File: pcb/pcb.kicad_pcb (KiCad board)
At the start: 2 copper layers, 55 x 70 mm, 61 parts, among them J1 SW, J2 HEATER, J3 FAN, J4 BME280, J5 DISPLAY, J6 NTC, J7 POWER, Q1 IRFR9024NTRPBF, Q2 2n3904S-RTK/PS_C18536, Q3 2n3904S-RTK/PS_C18536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

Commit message: Work with schematics and pcb. update *.ioc files at project.
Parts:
- removed C13: 100uf, Capacitor_THT:CP_Radial_D8.0mm_P5.00mm
- added H1: MountingHole, MountingHole:MountingHole_3.2mm_M3_DIN965_Pad, F.Cu at (94.2, 54.0)
- added H2: MountingHole, MountingHole:MountingHole_3.2mm_M3_DIN965_Pad, F.Cu at (62.0, 53.8)
- added H3: MountingHole, MountingHole:MountingHole_3.2mm_M3_DIN965_Pad, F.Cu at (95.1, 126.2)
- added H4: MountingHole, MountingHole:MountingHole_3.2mm_M3_DIN965_Pad, F.Cu at (61.6, 126.2)
- C10, C11, C12, C15, C16, C17, C6, C7, C9, R17, R18, R19, R4, U1, Y1: moved to B.Cu
- Q4, R16, R20, R6, R7: moved to F.Cu
- moved J4 49.7 mm to (60.5, 99.0)
- moved J6 44.9 mm to (95.1, 99.2), turned to 90 degrees
- moved R15 32.9 mm to (69.1, 98.7), turned to -90 degrees
- moved R6 29.5 mm to (72.7, 79.9), turned to 180 degrees
- moved R16 28.5 mm to (84.8, 104.0), turned to 180 degrees
- moved J1 27.1 mm to (71.7, 83.1), turned to -90 degrees
- moved J5 26.4 mm to (66.4, 94.9), turned to 90 degrees
- moved R14 25.8 mm to (71.4, 96.0), turned to -90 degrees
- moved J3 24.9 mm to (75.7, 75.2)
- moved SW3 24.7 mm to (71.4, 123.1), turned to 90 degrees
- moved BZ1 23.9 mm to (64.6, 118.8), turned to 45 degrees
- moved D1 23.5 mm to (95.6, 73.0), turned to -90 degrees
- moved R7 23.4 mm to (78.3, 79.9), turned to 180 degrees
- moved C12 20.4 mm to (72.0, 93.4), turned to 90 degrees
- moved Q4 19.9 mm to (66.7, 112.9), turned to 135 degrees
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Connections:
- J2 pad 1: GND -> Net-(D1-K)
- J2 pad 2: Net-(D1-K) -> GND
- J3 pad 1: GND -> Net-(D3-K)
- J3 pad 2: Net-(D3-K) -> GND
- J4 pad 1: +3.3V -> GND
- J4 pad 4: GND -> +3.3V
- J6 pad 1: GND -> /NTC
- J6 pad 2: /NTC -> GND
- U1 pad 16: /PWM_BUZZER -> unconnected-(U1-PA6-Pad16)
- U1 pad 29: /PWM_HEATER -> /PWM_BUZZER
- U1 pad 38: /PWM_FAN -> unconnected-(U1-PA15-Pad38)
- U1 pad 39: unconnected-(U1-PB3-Pad39) -> /PWM_HEATER
- U1 pad 40: unconnected-(U1-PB4-Pad40) -> /PWM_FAN
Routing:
- net +24V: track 9.62 -> 50.4 mm, vias 0 -> 2
- net /NTC: track 53.6 -> 17.8 mm
- net +3.3V: track 160.2 -> 125.3 mm
- net /SWDIO: track 11.8 -> 22.6 mm, vias 0 -> 1
- net Net-(Q2-B): track 2.32 -> 12.9 mm, vias 0 -> 2
- net /PWM_FAN: track 20.4 -> 30.9 mm, vias 1 -> 0
- net /PWM_HEATER: track 22.0 -> 14.2 mm, vias 1 -> 0
- net Net-(D1-K): track 0.00 -> 6.49 mm
- net /BTN_RIGHT: track 23.9 -> 29.6 mm, vias 0 -> 1
- net GND: track 34.1 -> 39.6 mm, vias 3 -> 4
- net /PWM_BUZZER: track 18.1 -> 12.6 mm
- net Net-(U1-NRST): track 11.6 -> 6.69 mm, vias 0 -> 1
- net Net-(Q2-C): track 2.17 -> 5.72 mm
- net /BTN_OK: track 26.1 -> 29.0 mm, vias 0 -> 1
- net Net-(BZ1-+): track 5.29 -> 2.58 mm
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- added copper zone on B.Cu, net Net-(D1-K)
- added copper zone on F.Cu, net Net-(D1-K)
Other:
- board size 55 x 70 mm -> 42 x 80 mm

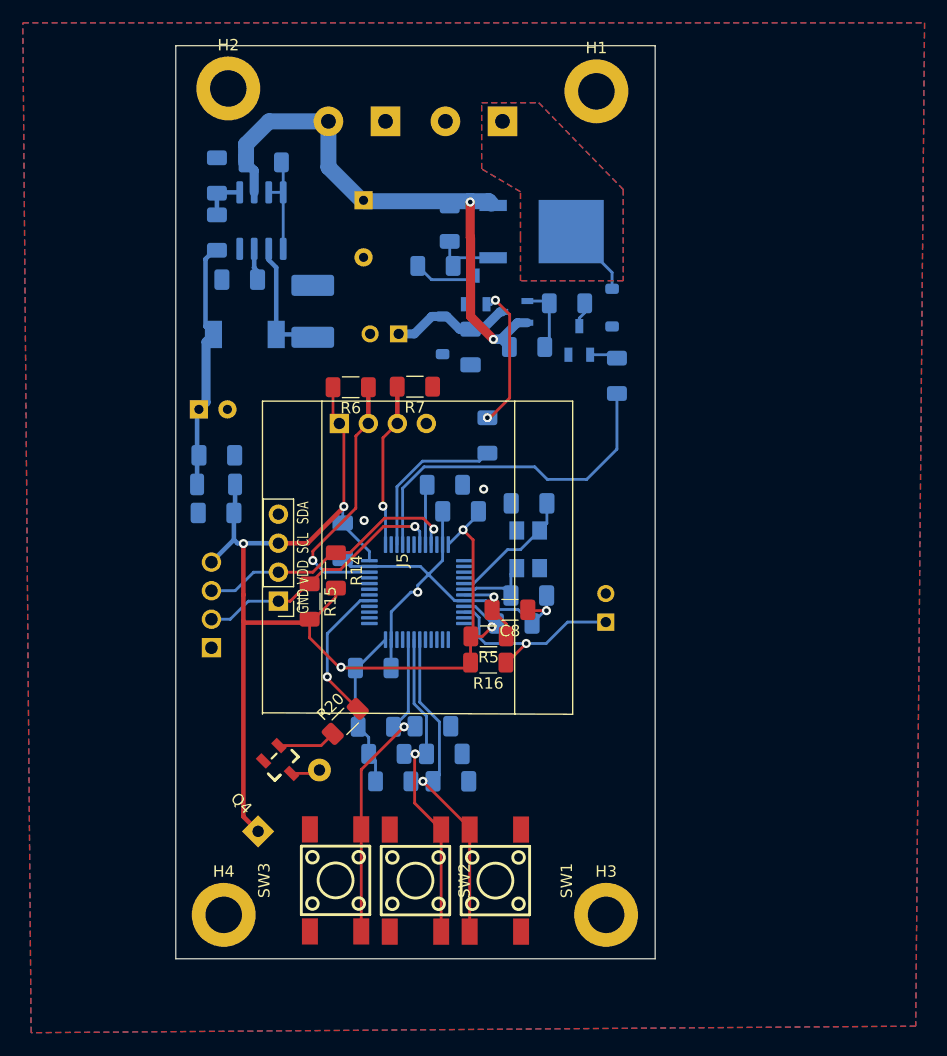
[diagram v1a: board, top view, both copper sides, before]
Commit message: Work in pcb placment components
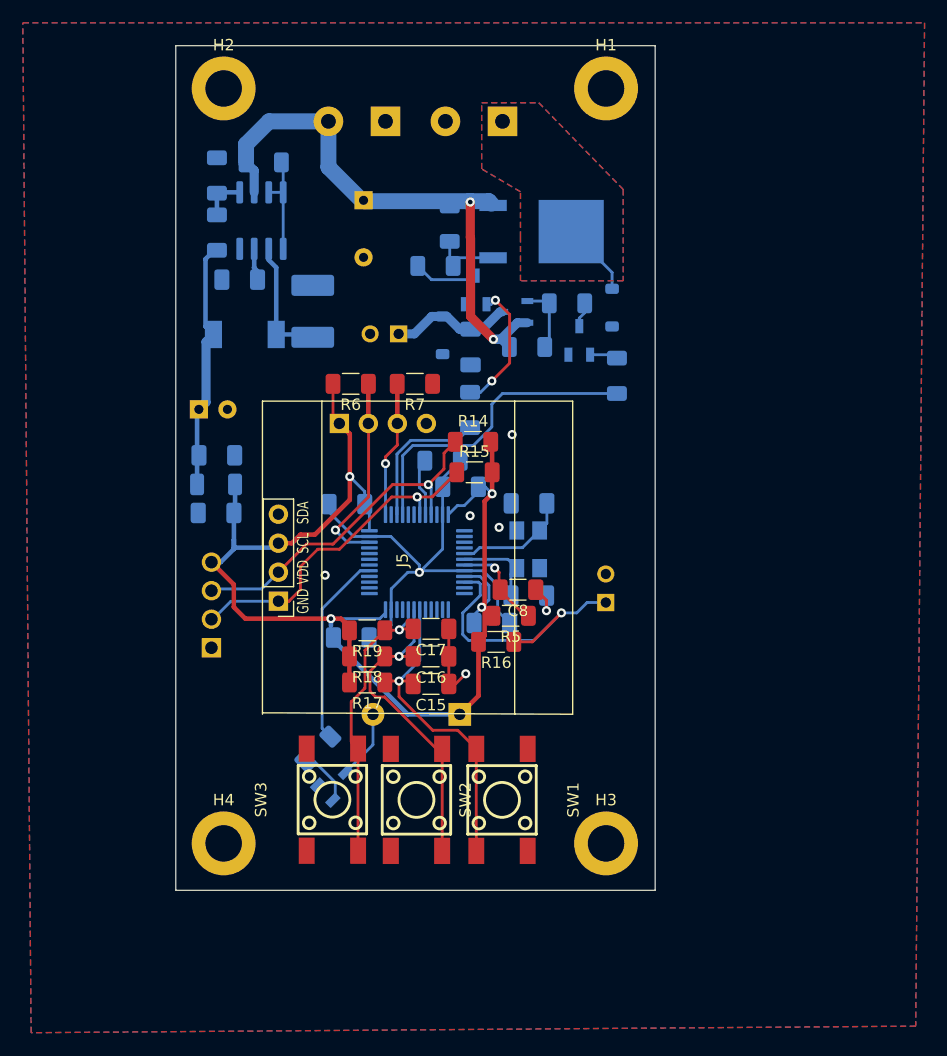
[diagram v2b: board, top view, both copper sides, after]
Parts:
- C15, C16, C17, R17, R18, R19: moved to F.Cu
- Q4, R20: moved to B.Cu
- moved BZ1 20.4 mm to (82.3, 108.6), turned to 180 degrees
- moved R15 18.4 mm to (83.6, 87.4), turned to 0 degrees
- moved R14 16.5 mm to (83.4, 84.7), turned to 0 degrees
- moved R17 8.95 mm to (74.2, 105.8)
- moved R18 8.71 mm to (74.2, 103.5)
- moved C15 8.71 mm to (79.8, 105.9)
- moved C16 8.62 mm to (79.8, 103.5)
- moved C17 8.53 mm to (79.8, 101.1)
- moved R19 8.49 mm to (74.2, 101.2)
- moved SW1 7.10 mm to (86.0, 116.1)
- moved SW3 7.08 mm to (71.1, 116.1)
- moved SW2 7.07 mm to (78.5, 116.1)
- moved H3 6.26 mm to (95.1, 119.9)
- moved H4 6.26 mm to (61.6, 119.9)
- moved Q4 5.01 mm to (71.4, 114.6), turned to -135 degrees
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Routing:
- net GND: track 39.6 -> 52.5 mm, vias 4 -> 7
- net +3.3V: track 125.3 -> 113.3 mm, vias 5 -> 4
- net /NTC: track 17.8 -> 25.9 mm
- net /SDA: track 23.3 -> 29.7 mm
- net /SCL: track 24.0 -> 30.3 mm
- net /SWDIO: track 22.6 -> 17.5 mm
- net /PWM_BUZZER: track 12.6 -> 17.0 mm, vias 1 -> 0
- net /BTN_RIGHT: track 29.6 -> 25.4 mm
- net /PWM_FAN: track 30.9 -> 27.4 mm
- net Net-(BZ1-+): track 2.58 -> 6.09 mm
- net /SWCLK: track 14.5 -> 11.9 mm
- net Net-(U1-NRST): track 6.69 -> 8.34 mm
- net /PWM_HEATER: track 14.2 -> 12.7 mm
- net /BTN_LEFT: track 30.2 -> 28.8 mm
- net Net-(Q2-B): track 12.9 -> 11.7 mm
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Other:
- board size 42 x 80 mm -> 42 x 74 mm

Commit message: Update display ss1306 footprint. paste text refrenece on pcb
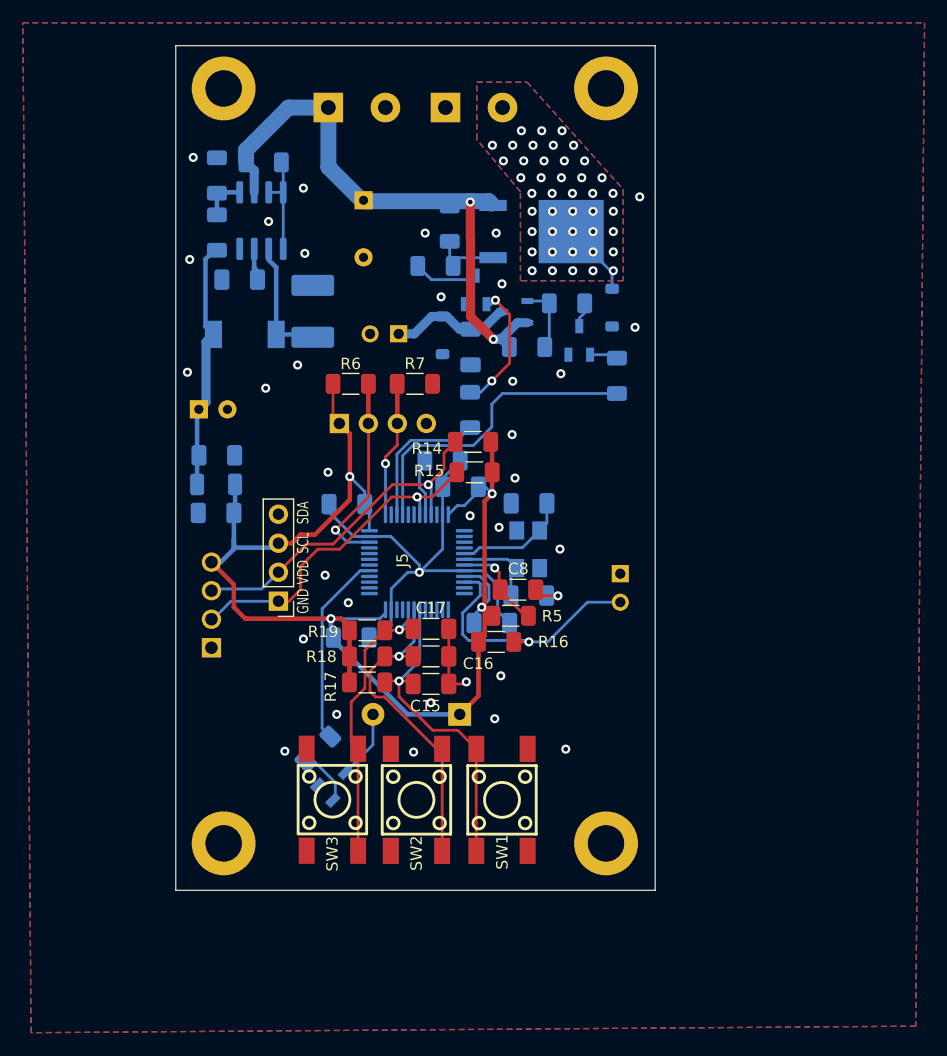
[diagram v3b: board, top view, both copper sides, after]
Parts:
- moved J7 5.15 mm to (70.8, 55.4), turned to 0 degrees
- moved J2 5.14 mm to (81.0, 55.4), turned to 0 degrees
- moved J6 1.27 mm to (96.3, 97.5), turned to -90 degrees
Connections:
- J2 pad 1: Net-(D1-K) -> GND
- J2 pad 2: GND -> Net-(D1-K)
- J6 pad 1: /NTC -> GND
- J6 pad 2: GND -> /NTC
- J7 pad 1: GND -> +24V
- J7 pad 2: +24V -> GND
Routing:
- net /NTC: track 25.9 -> 23.4 mm
- net +24V: track 50.4 -> 51.8 mm
- net GND: track 52.5 -> 51.8 mm, vias 7 -> 35
- net Net-(D1-K): vias 0 -> 43
